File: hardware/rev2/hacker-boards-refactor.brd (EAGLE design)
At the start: 30.7 x 58.4 mm, 38 parts, among them J1 MICRO_USB_B_JST_MC5BR3-M404-4S

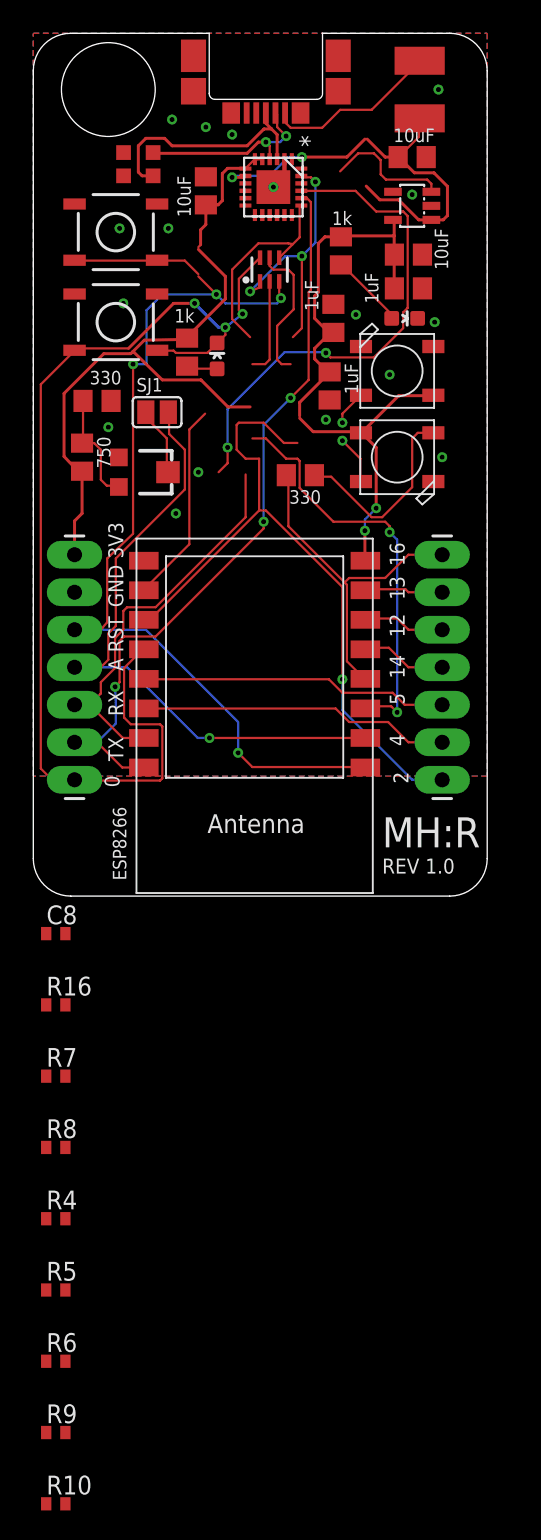
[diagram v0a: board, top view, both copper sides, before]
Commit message: Shrank the board and re-placed components, looking for an optimized second prototyping run
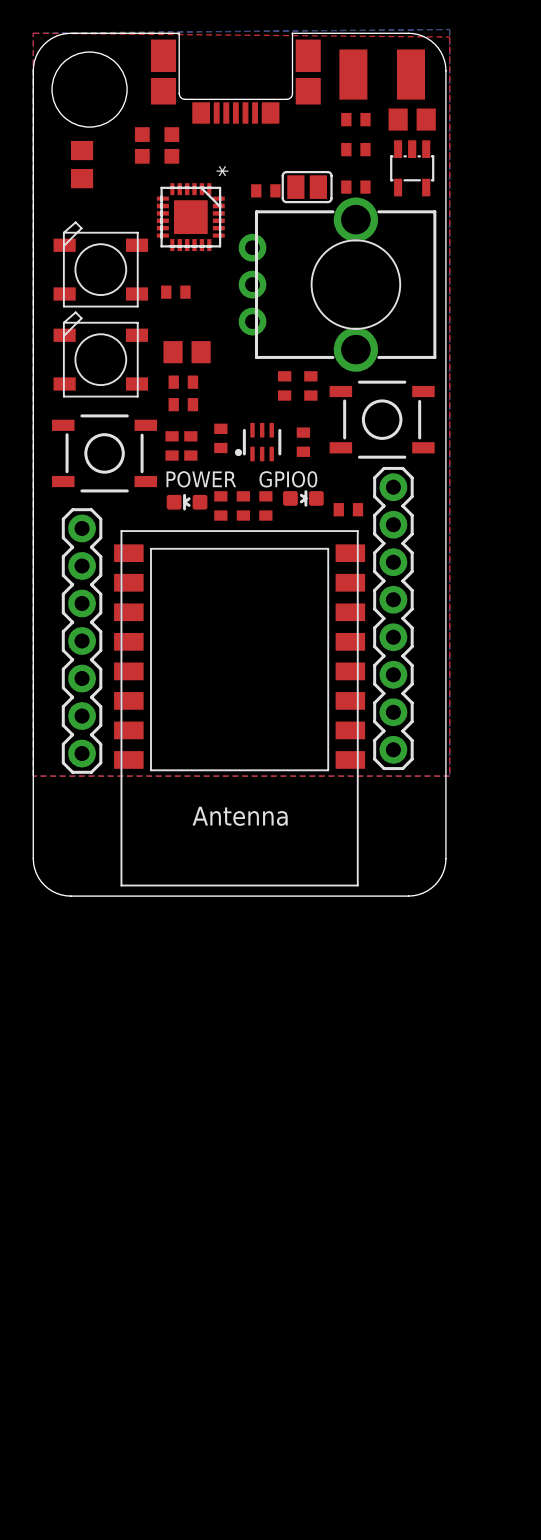
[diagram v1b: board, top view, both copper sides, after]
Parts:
- removed C3: 1uF, hacker-board:C0805
- removed JP2: (no value), hacker-board:1X07_LONGPADS
- removed R11: 330, resistor:R0805
- removed TM1: (no value), adafruit:TC33X
- added C4: 1uF, resistor:C0402
- added JP3: (no value), SparkFun-Connectors:1X07
- added R2: 750, resistor:R0402
- added RV1: (no value), SparkFun-Electromechanical:ALPS_POT_KIT
- C6, C7: device hacker-board:C0805 -> resistor:C0402
- JP1: device hacker-board:1X07_LONGPADS -> SparkFun-Connectors:1X08_ROUND
- R1, R15, R3: device resistor:R0805 -> resistor:R0402
- R14: value 750 -> 330; device resistor:R0805 -> resistor:R0402
- moved R10 72.1 mm to (9.40, 30.5), turned to 90 degrees
- moved R9 69.1 mm to (18.3, 30.7), turned to 270 degrees
- moved R7 65.9 mm to (21.8, 50.5)
- moved R6 63.5 mm to (12.7, 31.0), turned to 90 degrees
- moved C8 58.7 mm to (21.8, 52.6), turned to 180 degrees
- moved R16 56.9 mm to (15.7, 47.8), turned to 180 degrees
- moved R5 54.2 mm to (12.7, 26.4), turned to 270 degrees
- moved R4 50.3 mm to (15.7, 26.4), turned to 90 degrees
- moved R8 45.3 mm to (14.2, 26.4), turned to 90 degrees
- moved JP1 29.3 mm to (24.4, 27.7), turned to 270 degrees
- moved LED2 21.2 mm to (4.57, 42.4)
- moved LED1 21.1 mm to (4.57, 36.3), turned to 0 degrees
- moved S2 19.2 mm to (23.6, 32.3)
- moved SJ1 18.3 mm to (18.5, 48.0)
- moved R1 17.5 mm to (21.3, 26.2), turned to 0 degrees
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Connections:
- net +3V3: now also C4.1, JP3.7, R2.2; no longer C3.1, JP1.7, R14.2
- net ANALOG_IN: now also JP3.4; no longer JP1.4
- net GND: now also C4.2, JP3.6, R14.1, RV1.P$3; no longer C3.2, JP1.6, R15.1, TM1.1
- net GPIO0: now also JP3.1; no longer JP1.1
- net GPIO12: now also JP1.4; no longer JP2.3
- net GPIO13: now also JP1.3; no longer JP2.2
- net GPIO14: now also JP1.5; no longer JP2.4
- net GPIO15: now also JP1.2, R15.2
- net GPIO16: now also JP1.1; no longer JP2.1, R11.2
- net GPIO2: now also JP1.8; no longer JP2.7
- net GPIO4/SDA: now also JP1.7; no longer JP2.6
- net GPIO5/SCL: now also JP1.6; no longer JP2.5
- net N$12: now also RV1.P$2; no longer TM1.2
- net N$4: now also R14.2, R2.1, RV1.P$1; no longer R14.1, R15.2, TM1.3
- net N$6: now also R15.1; no longer R11.1
- net RST: now also JP3.5; no longer JP1.5
- net RX: now also JP3.3; no longer JP1.3
- net TX: now also JP3.2; no longer JP1.2
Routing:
- net +3V3: track 93.1 -> 0.00 mm, vias 2 -> 0
- net GPIO0: track 73.6 -> 0.00 mm, vias 3 -> 0
- net RST: track 71.7 -> 0.00 mm, vias 4 -> 0
- net TX: track 51.5 -> 0.00 mm, vias 3 -> 0
- net GPIO2: track 47.4 -> 0.00 mm, vias 1 -> 0
- net ANALOG_IN: track 43.6 -> 0.00 mm, vias 1 -> 0
- net USB_RX: track 34.6 -> 0.00 mm, vias 2 -> 0
- net +5V: track 29.5 -> 0.00 mm, vias 2 -> 0
- net CH_PD: track 28.0 -> 0.00 mm, vias 2 -> 0
- net RX: track 27.2 -> 0.00 mm
- net GPIO16: track 23.5 -> 0.00 mm
- net GPIO4/SDA: track 21.1 -> 0.00 mm
- net GPIO5/SCL: track 20.9 -> 0.00 mm
- net DTR: track 17.9 -> 0.00 mm, vias 3 -> 0
- net USB+: track 16.3 -> 0.00 mm
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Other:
- board size 30.7 x 58.4 mm -> 27.9 x 58.4 mm
- board text added: "GPIO0"
- board text added: "POWER"
- board text removed: "0"
- board text removed: "12"
- board text removed: "13"
- board text removed: "14"
- board text removed: "16"
- board text removed: "2"
- board text removed: "3V3"
- board text removed: "4"
- board text removed: "5"
- board text removed: "A"
- board text removed: "ESP8266"
- board text removed: "GND"
- board text removed: "Jonathan Zarger Colin Szechy"
- board text removed: "MH:R"
- board text removed: "MHACKS: REFACTOR HACKER BOARD"
- board text removed: "PLACE NFC HERE"
- board text removed: "REV 1.0"
- board text removed: "RST"
- board text removed: "RX"
- board text removed: "TX"

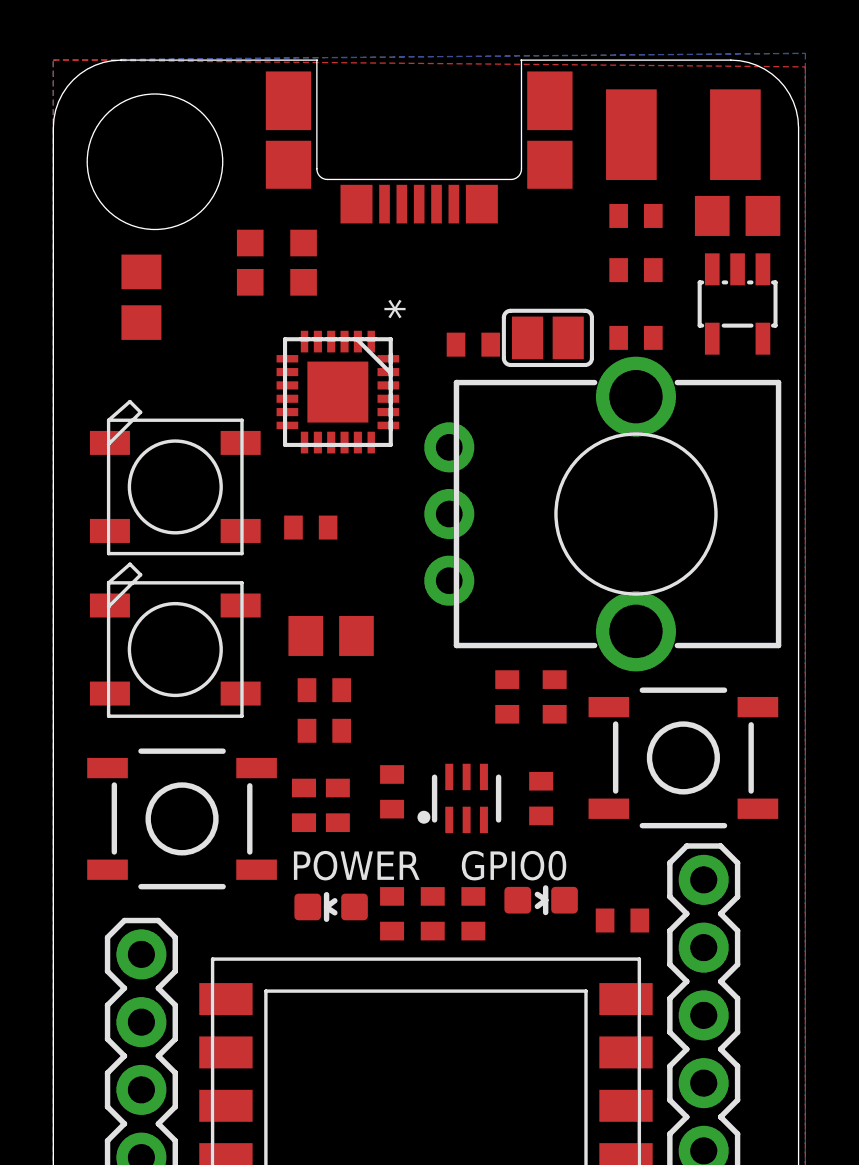
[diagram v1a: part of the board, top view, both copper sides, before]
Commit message: Added 5V/3V3 traces
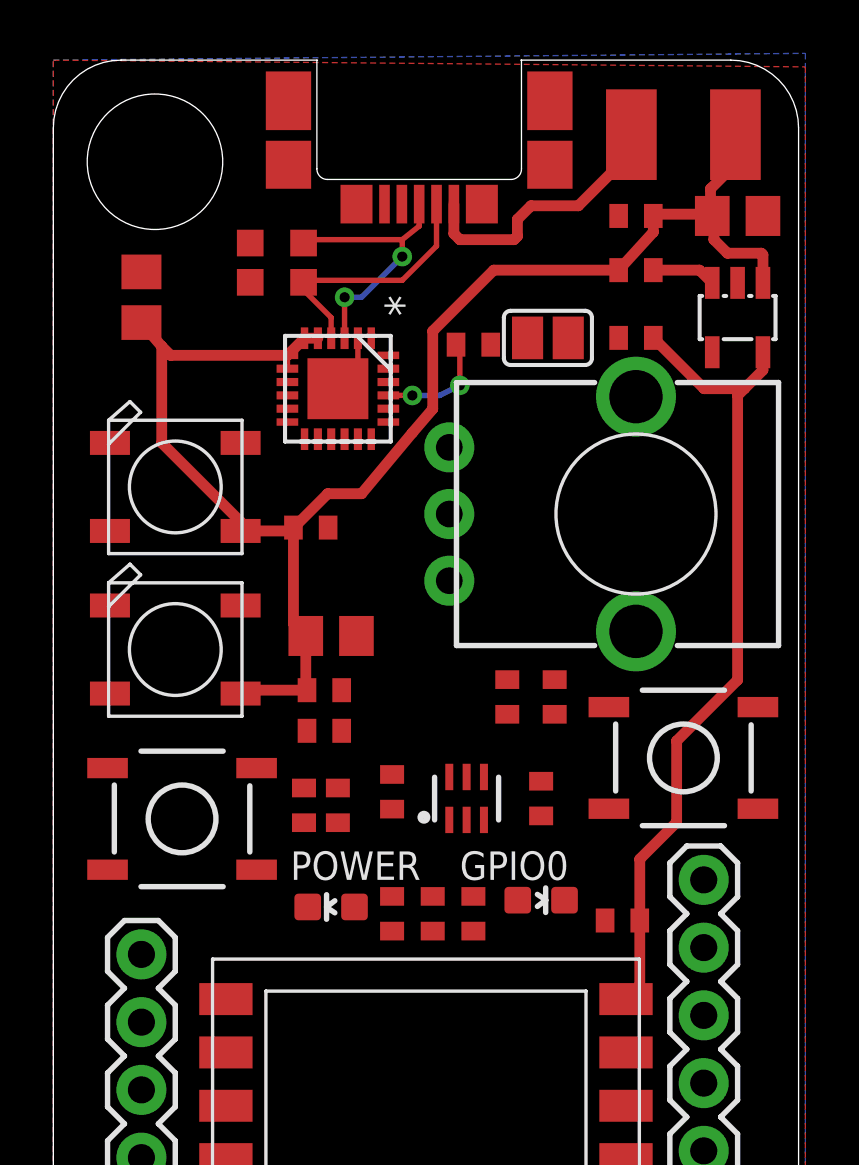
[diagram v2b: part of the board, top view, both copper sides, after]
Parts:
- moved U$2 0.51 mm to (25.7, 48.8)
- moved U$3 0.13 mm to (10.7, 46.1)
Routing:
- net +3V3: track 0.00 -> 57.7 mm
- net +5V: track 0.00 -> 31.3 mm
- net N$2: track 0.00 -> 10.4 mm
- net USB+: track 0.00 -> 10.4 mm, vias 0 -> 2
- net USB-: track 0.00 -> 9.64 mm
- net USB_RX: track 0.00 -> 4.32 mm, vias 0 -> 2
- net N$7: track 0.00 -> 2.41 mm
- net GND: track 0.00 -> 2.20 mm

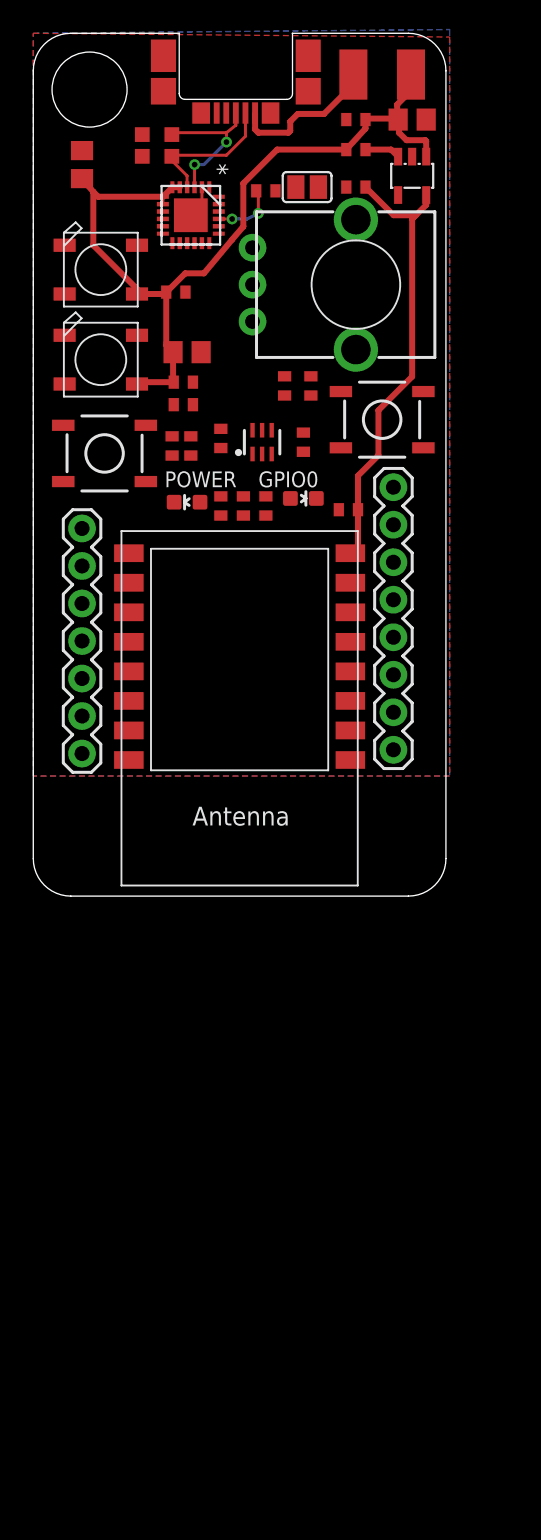
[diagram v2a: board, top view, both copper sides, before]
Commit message: Removed fuse, played around/shrunk board dimensions some more
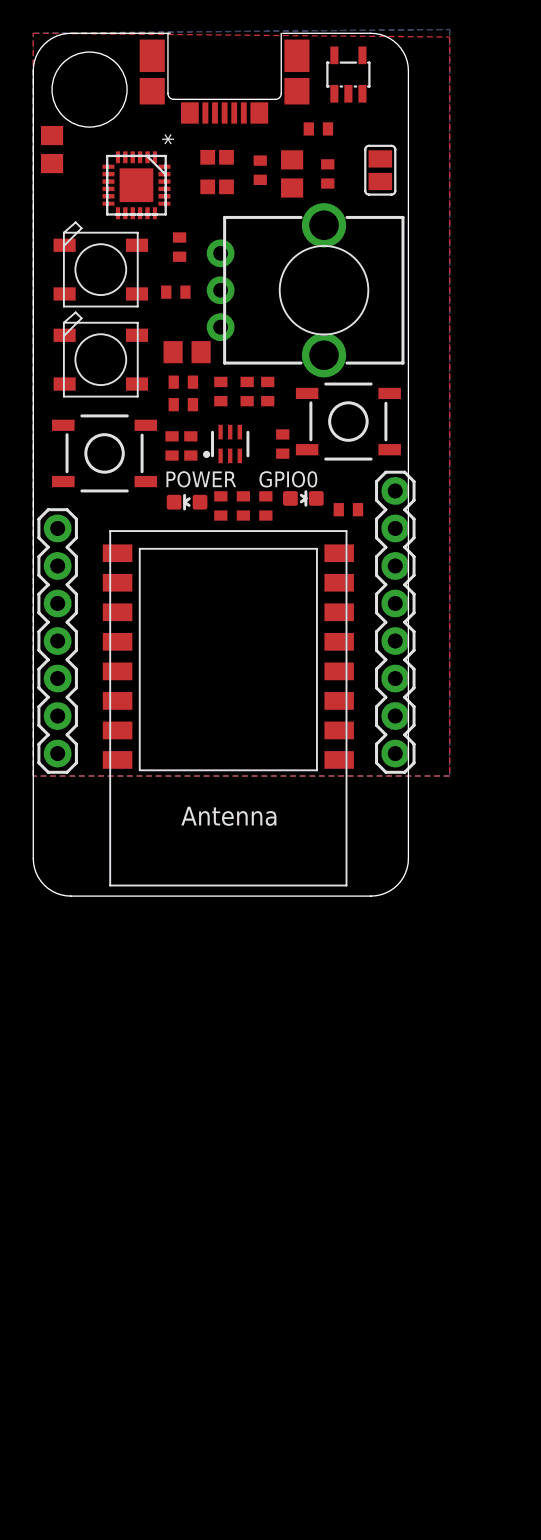
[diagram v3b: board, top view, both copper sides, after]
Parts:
- removed U$1: USB-FUSE, hacker-board:L1812
- moved C1 8.92 mm to (17.5, 48.9), turned to 270 degrees
- moved U$2 8.10 mm to (21.3, 55.6), turned to 0 degrees
- moved C8 7.33 mm to (15.4, 49.1), turned to 270 degrees
- moved R16 6.97 mm to (9.91, 43.9), turned to 90 degrees
- moved SJ1 5.08 mm to (23.5, 49.1), turned to 270 degrees
- moved R13 4.82 mm to (13.1, 49.0), turned to 270 degrees
- moved R12 4.27 mm to (11.8, 49.0), turned to 270 degrees
- moved U$3 4.21 mm to (6.99, 48.1)
- moved R6 3.17 mm to (12.7, 34.2)
- moved R2 2.95 mm to (15.9, 34.2)
- moved R7 2.90 mm to (19.3, 51.9)
- moved R14 2.57 mm to (14.5, 34.2)
- moved S2 2.29 mm to (21.3, 32.1)
- moved C5 2.27 mm to (1.27, 50.5)
- moved RV1 2.19 mm to (19.7, 41.0)
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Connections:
- removed net N$2: J1.1, U$1.1
- net +5V: now also J1.1; no longer U$1.2
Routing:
- net +3V3: track 57.7 -> 0.00 mm
- net +5V: track 31.3 -> 0.00 mm
- net N$2: track 10.4 -> 0.00 mm
- net USB+: track 10.4 -> 0.00 mm, vias 2 -> 0
- net USB-: track 9.64 -> 0.00 mm
- net USB_RX: track 4.32 -> 0.00 mm, vias 2 -> 0
- net N$7: track 2.41 -> 0.00 mm
- net GND: track 2.20 -> 0.00 mm
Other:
- board size 27.9 x 58.4 mm -> 25.4 x 58.4 mm
- board text added: "POT-SJ"

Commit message: First pass at routing
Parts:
- moved R12 1.33 mm to (11.4, 47.8)
- moved R13 1.33 mm to (13.5, 47.8)
- moved U$3 1.20 mm to (7.37, 49.3), turned to 0 degrees
- moved JP1 0.38 mm to (24.1, 27.4)
- moved JP3 0.38 mm to (1.27, 24.9)
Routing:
- net GND: track 0.00 -> 210.1 mm, vias 0 -> 6
- net +3V3: track 0.00 -> 154.4 mm, vias 0 -> 3
- net ANALOG_IN: track 0.00 -> 91.3 mm, vias 0 -> 3
- net GPIO0: track 0.00 -> 69.9 mm, vias 0 -> 5
- net RST: track 0.00 -> 60.6 mm, vias 0 -> 4
- net RX: track 0.00 -> 56.0 mm, vias 0 -> 3
- net GPIO15: track 0.00 -> 54.6 mm, vias 0 -> 2
- net TX: track 0.00 -> 51.9 mm, vias 0 -> 3
- net DTR: track 0.00 -> 38.1 mm
- net GPIO2: track 0.00 -> 32.5 mm, vias 0 -> 1
- net RTS: track 0.00 -> 27.9 mm, vias 0 -> 2
- net USB_RX: track 0.00 -> 26.9 mm, vias 0 -> 2
- net GPIO4/SDA: track 0.00 -> 22.9 mm
- net +5V: track 0.00 -> 22.7 mm
- net GPIO5/SCL: track 0.00 -> 20.8 mm
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- removed copper zone on layer 1, net GND
- removed copper zone on layer 16, net GND

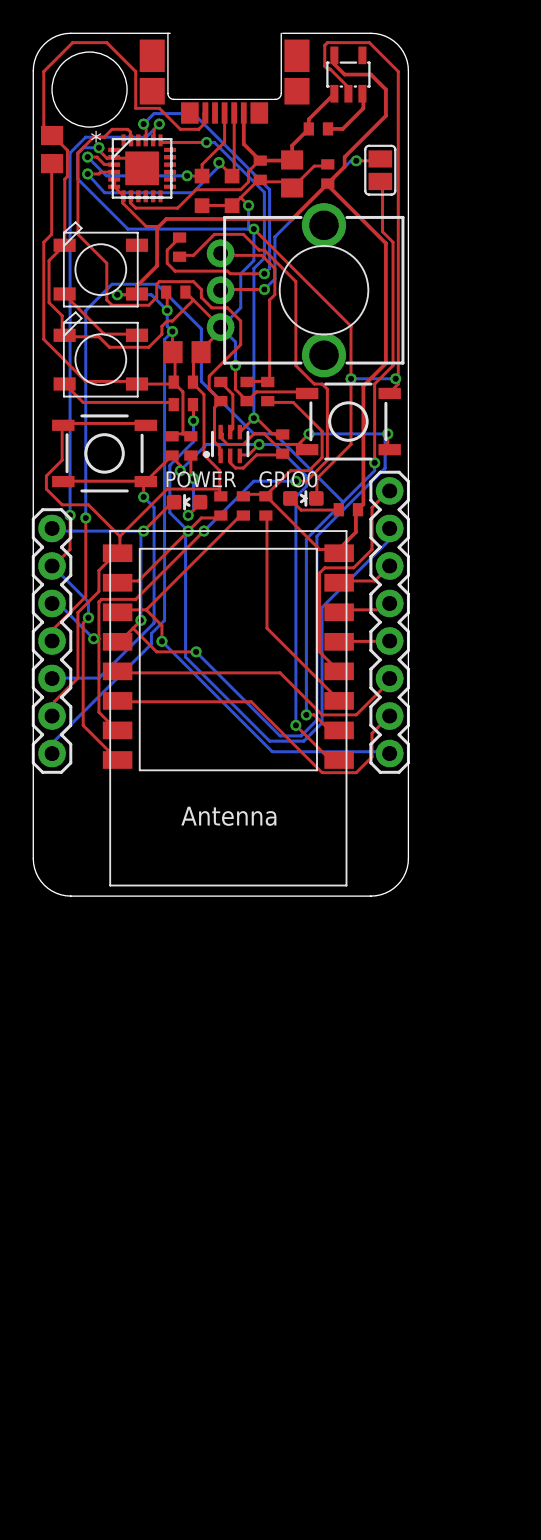
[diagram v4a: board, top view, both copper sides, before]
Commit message: Added polygons/planes to board
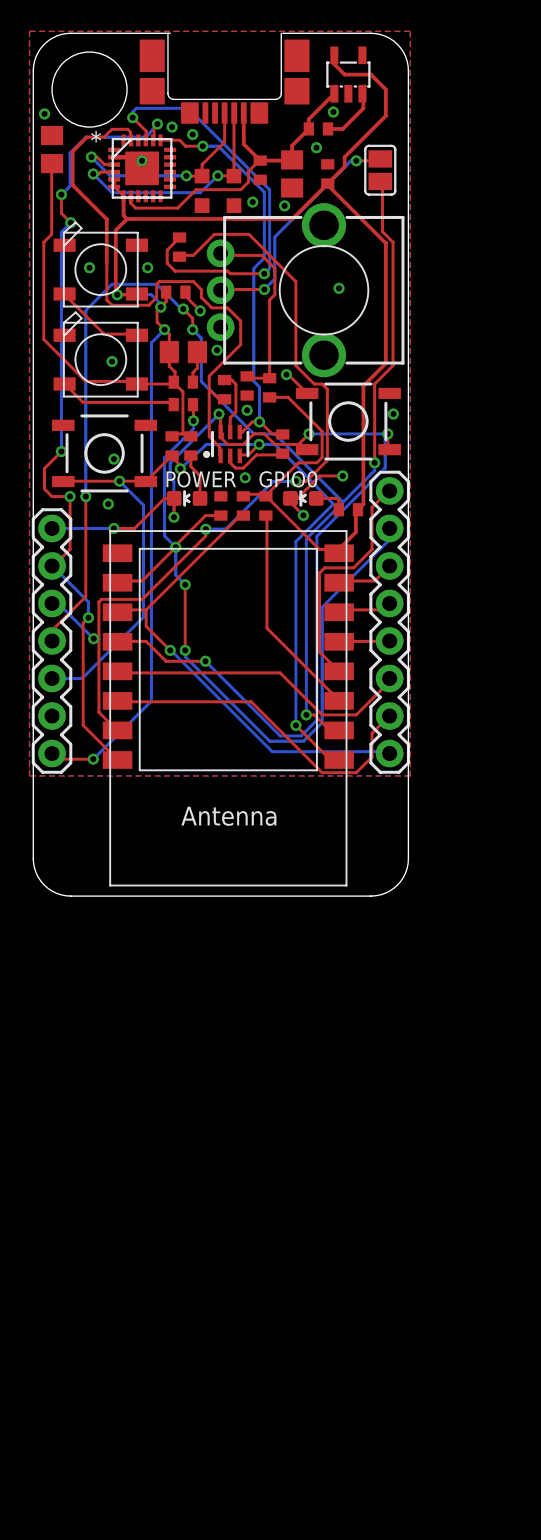
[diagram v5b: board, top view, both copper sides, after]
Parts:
- moved R14 0.38 mm to (14.5, 34.5)
- moved R2 0.28 mm to (16.0, 34.4)
- moved R6 0.28 mm to (13.0, 34.3)
- moved C2 0.25 mm to (10.2, 36.8)
- moved D2 0.25 mm to (10.4, 26.9)
- moved R13 0.13 mm to (13.6, 47.8)
- turned D1 to 90 degrees
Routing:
- net GND: track 210.1 -> 13.6 mm, vias 6 -> 22
- net GPIO0: track 69.9 -> 73.8 mm, vias 5 -> 6
- net TX: track 51.9 -> 54.5 mm, vias 3 -> 6
- net +3V3: track 154.4 -> 156.9 mm, vias 3 -> 4
- net N$3: track 5.62 -> 3.16 mm, vias 2 -> 0
- net USB_RX: track 26.9 -> 28.8 mm
- net USB-: track 17.9 -> 16.3 mm
- net DTR: track 38.1 -> 39.8 mm
- net N$1: track 3.64 -> 2.30 mm
- net RST: track 60.6 -> 61.6 mm
- net N$11: track 3.80 -> 4.59 mm
- net USB+: track 15.2 -> 14.7 mm
- net GPIO15: track 54.6 -> 54.7 mm, vias 2 -> 4
- net ANALOG_IN: track 91.3 -> 91.4 mm, vias 3 -> 5
- added copper zone on layer 1, net GND
- added copper zone on layer 16, net GND
